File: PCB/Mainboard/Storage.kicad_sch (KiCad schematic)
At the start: 46 parts, among them Q37 BH, U27 AT29LV512, U41 SDBL-4, U42 SC414281PU4, U56 SN74LV32, U65 E4, U68 SN74LV08

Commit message: Add files via upload
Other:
- company: (none) -> Recreated by: Ahmad Byagowi
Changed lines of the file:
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@@
 	(title_block
 		(title "PC110")
+		(company "Recreated by: Ahmad Byagowi")
 	)
 	(junction

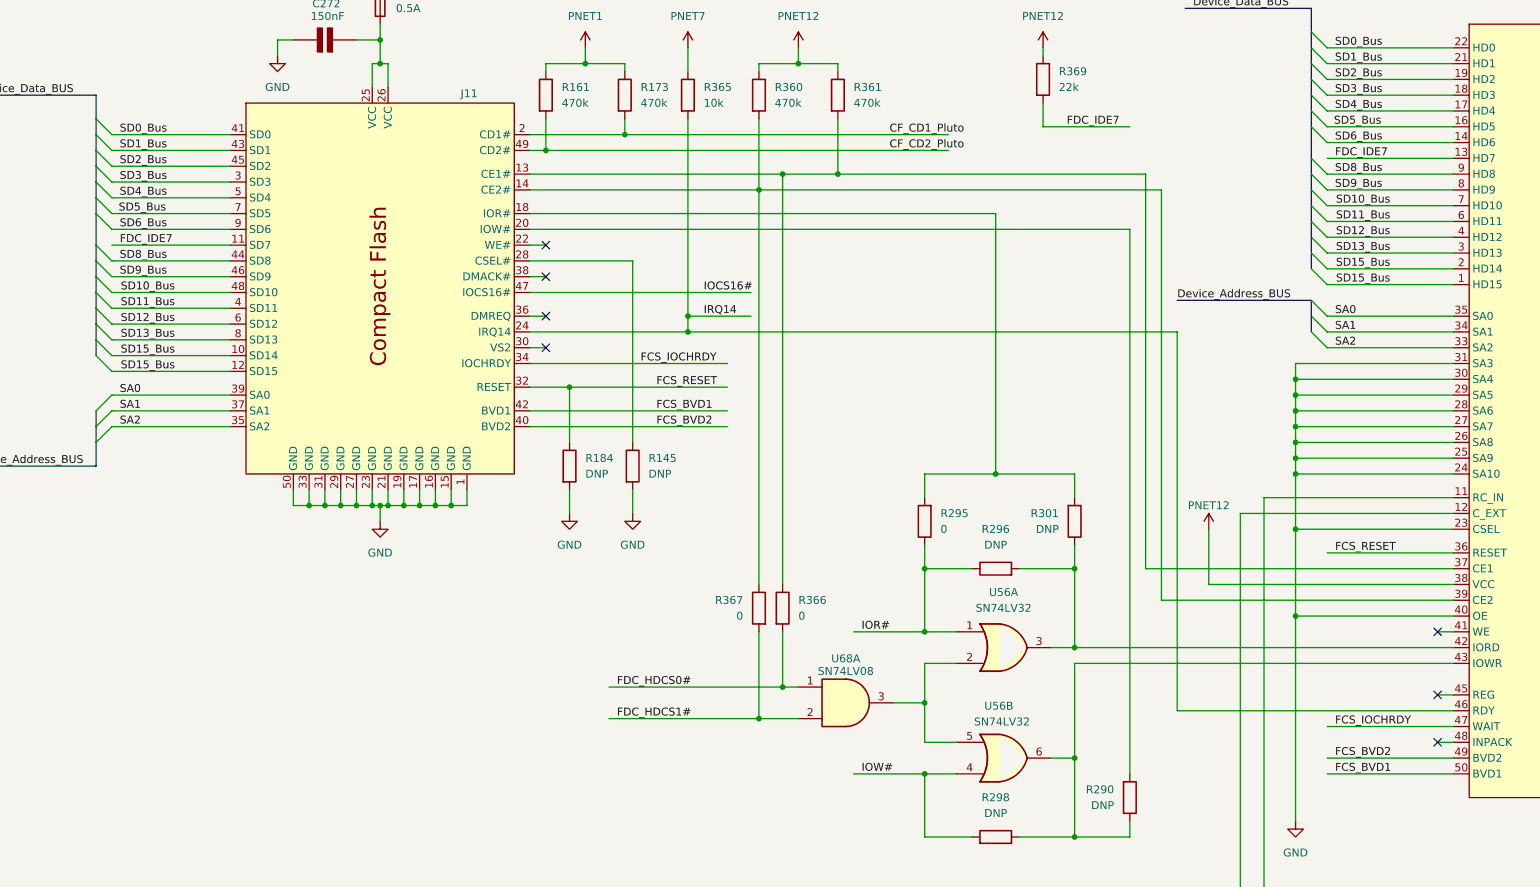
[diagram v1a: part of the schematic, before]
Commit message: Add part numbers to some SMT parts
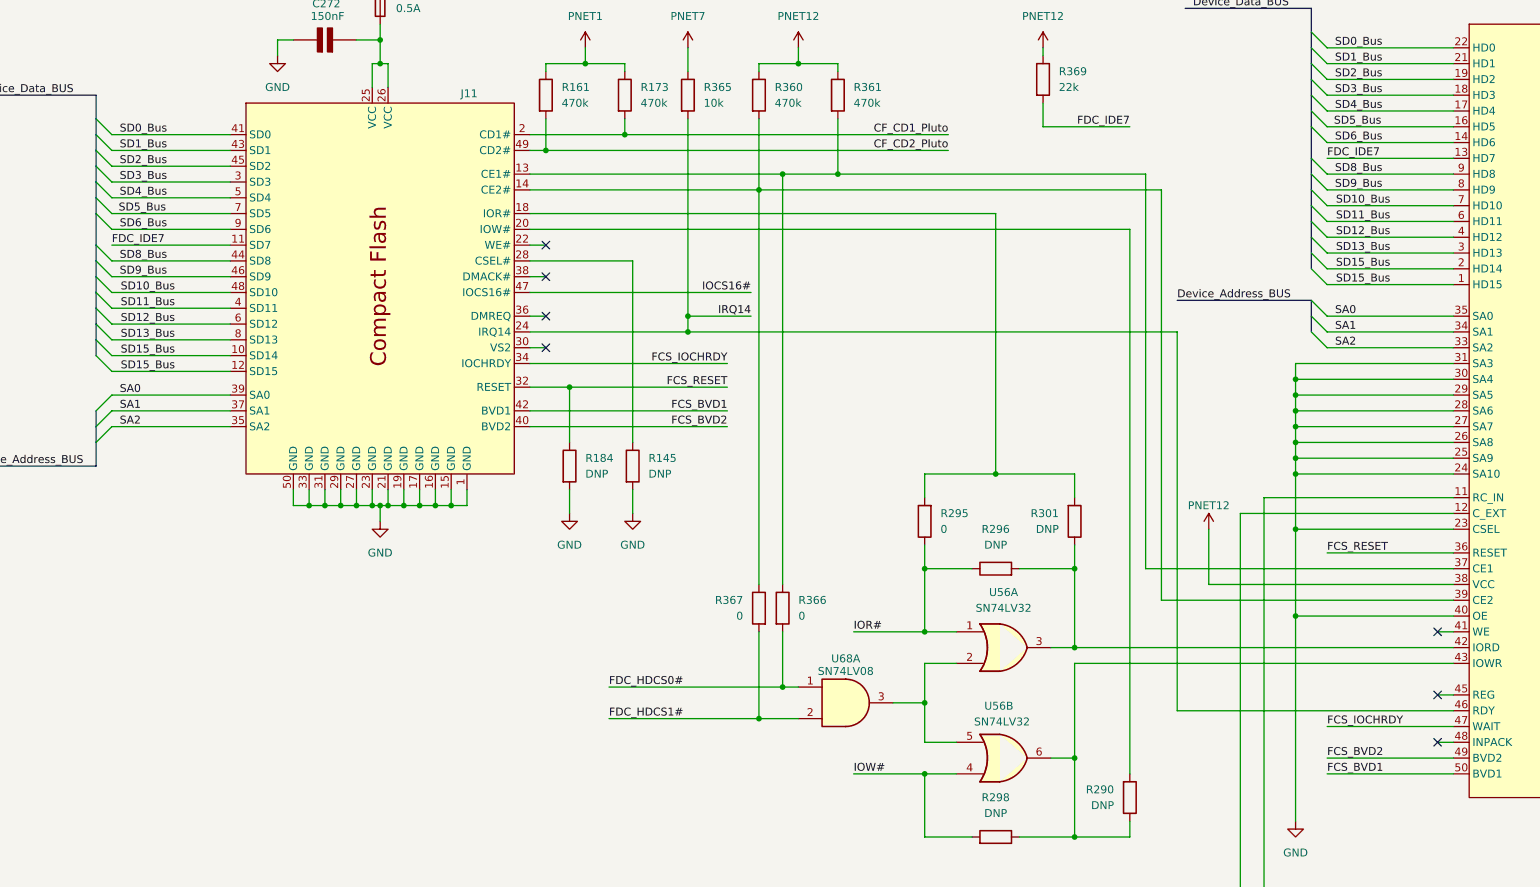
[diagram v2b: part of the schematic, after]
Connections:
- net CF_CD1_Pluto: now also J11.2 (CD1#), R173.2
- net CF_CD2_Pluto: now also J11.49 (CD2#), R161.2
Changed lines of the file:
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@@
 	)
 	(label "CF_CD1_Pluto"
-		(at 191.77 130.81 180)
+		(at 189.23 130.81 180)
 		(effects
 			(font
@@
 	)
 	(label "FDC_IDE7"
-		(at 55.88 148.59 0)
+		(at 54.61 148.59 0)
 		(effects
 			(font
@@
 	)
 	(label "FDC_IDE7"
-		(at 208.28 129.54 0)
-		(effects
-			(font
-				(size 1.27 1.27)
-			)
-			(justify left bottom)
+		(at 218.44 129.54 180)
+		(effects
+			(font
+				(size 1.27 1.27)
+			)
+			(justify right bottom)
 		)
 	)
@@
 	)
 	(label "FDC_HDCS1#"
-		(at 135.89 224.79 0)
+		(at 134.62 224.79 0)
 		(effects
 			(font
@@
 	)
 	(label "FCS_BVD1"
-		(at 142.24 175.26 0)
-		(effects
-			(font
-				(size 1.27 1.27)
-			)
-			(justify left bottom)
+		(at 153.67 175.26 180)
+		(effects
+			(font
+				(size 1.27 1.27)
+			)
+			(justify right bottom)
 		)
 	)
 	(label "FCS_IOCHRDY"
-		(at 139.7 167.64 0)
-		(effects
-			(font
-				(size 1.27 1.27)
-			)
-			(justify left bottom)
+		(at 153.67 167.64 180)
+		(effects
+			(font
+				(size 1.27 1.27)
+			)
+			(justify right bottom)
 		)
 	)
@@
 	)
 	(label "FCS_BVD1"
-		(at 251.46 233.68 0)
+		(at 250.19 233.68 0)
 		(effects
 			(font
@@
 	)
 	(label "FCS_RESET"
-		(at 142.24 171.45 0)
-		(effects
-			(font
-				(size 1.27 1.27)
-			)
-			(justify left bottom)
+		(at 153.67 171.45 180)
+		(effects
+			(font
+				(size 1.27 1.27)
+			)
+			(justify right bottom)
 		)
 	)
@@
 	)
 	(label "IRQ14"
-		(at 149.86 160.02 0)
-		(effects
-			(font
-				(size 1.27 1.27)
-			)
-			(justify left bottom)
+		(at 157.48 160.02 180)
+		(effects
+			(font
+				(size 1.27 1.27)
+			)
+			(justify right bottom)
 		)
 	)
@@
 	)
 	(label "FCS_BVD2"
-		(at 251.46 231.14 0)
+		(at 250.19 231.14 0)
 		(effects
 			(font
@@
 	)
 	(label "FCS_RESET"
-		(at 251.46 198.12 0)
+		(at 250.19 198.12 0)
 		(effects
 			(font
@@
 	)
 	(label "IOW#"
-		(at 175.26 233.68 0)
+		(at 173.99 233.68 0)
 		(effects
 			(font
@@
 	)
 	(label "IOR#"
-		(at 175.26 210.82 0)
+		(at 173.99 210.82 0)
 		(effects
 			(font
@@
 	)
 	(label "FDC_HDCS0#"
-		(at 135.89 219.71 0)
+		(at 134.62 219.71 0)
 		(effects
 			(font
@@
 	)
 	(label "FCS_IOCHRDY"
-		(at 251.46 226.06 0)
+		(at 250.19 226.06 0)
 		(effects
 			(font
@@
 	)
 	(label "FCS_BVD2"
-		(at 142.24 177.8 0)
-		(effects
-			(font
-				(size 1.27 1.27)
-			)
-			(justify left bottom)
+		(at 153.67 177.8 180)
+		(effects
+			(font
+				(size 1.27 1.27)
+			)
+			(justify right bottom)
 		)
 	)
@@
 	)
 	(label "CF_CD2_Pluto"
-		(at 191.77 133.35 180)
+		(at 189.23 133.35 180)
 		(effects
 			(font
@@
 	)
 	(label "FDC_IDE7"
-		(at 251.46 134.62 0)
+		(at 250.19 134.62 0)
 		(effects
 			(font
@@
 	)
 	(label "IOCS16#"
-		(at 149.86 156.21 0)
-		(effects
-			(font
-				(size 1.27 1.27)
-			)
-			(justify left bottom)
-		)
-	)
+		(at 157.48 156.21 180)
+		(effects
+			(font
+				(size 1.27 1.27)
+			)
+			(justify right bottom)
+		)
+	)
